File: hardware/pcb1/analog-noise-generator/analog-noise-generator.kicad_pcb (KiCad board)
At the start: 2 copper layers, 12.7 x 55.8 mm, 54 parts, among them J1 USB_C_Receptacle_USB2.0, J2 Conn_01x03, J5 Conn_01x04_Pin, J6 Conn_01x04_Pin, J7 Conn_01x02_Pin, U1 STM32F072CBTx, U2 USBLC6-2SC6, U3 LR8321A-T33, U4 LIS2DH12, U5 LM324

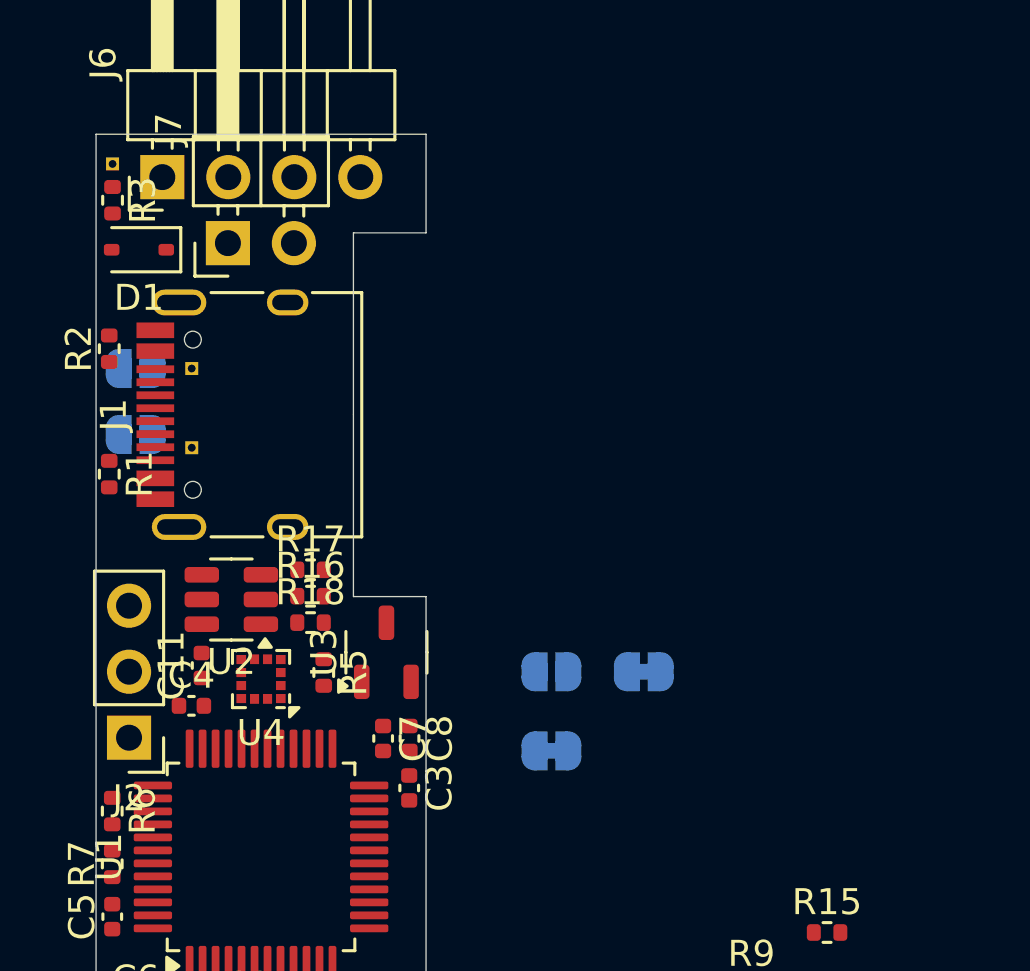
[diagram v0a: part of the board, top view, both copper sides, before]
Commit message: fix some violations
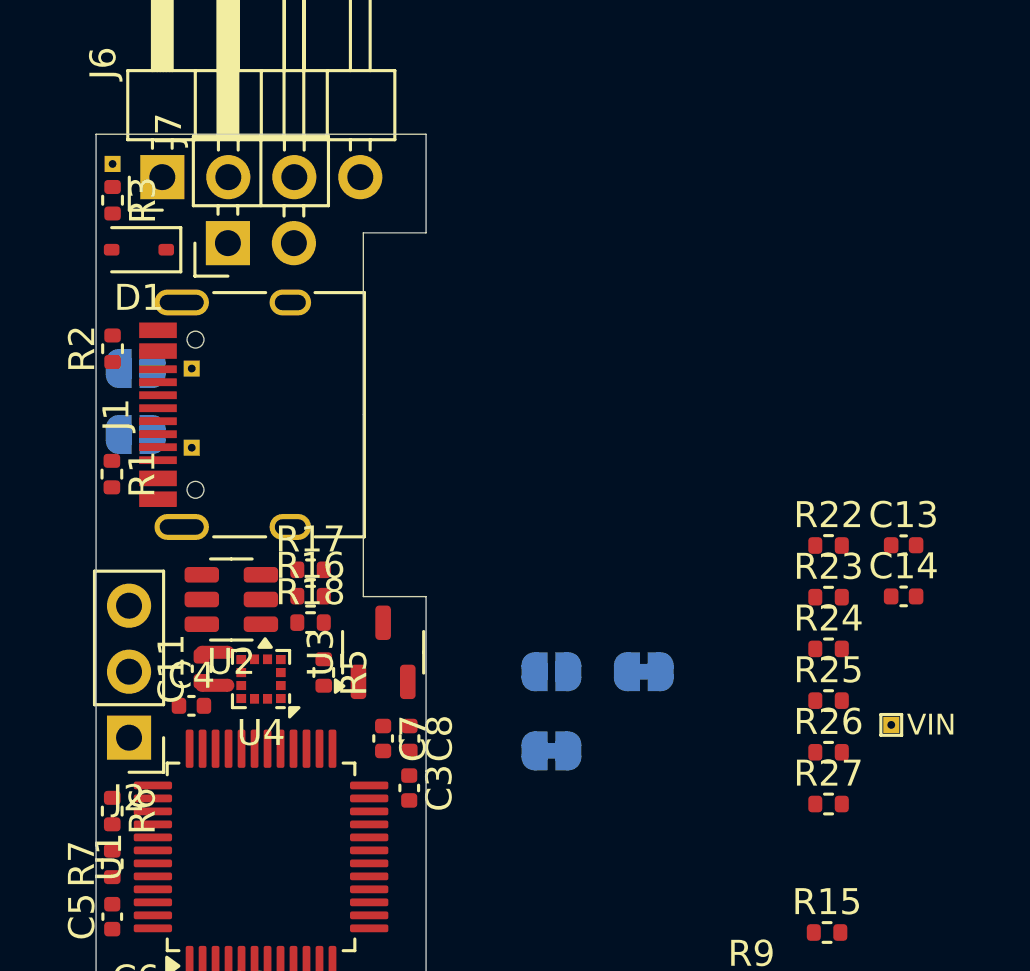
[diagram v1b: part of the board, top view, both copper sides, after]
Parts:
- added C13: 220p, Capacitor_SMD:C_0402_1005Metric, F.Cu at (136.5, 69.5)
- added C14: 220p, Capacitor_SMD:C_0402_1005Metric, F.Cu at (136.5, 71.5)
- added NT1: NetTie_2, NetTie:NetTie-2_SMD_Pad0.5mm, F.Cu at (110.0, 73.7)
- added NT2: NetTie_2, NetTie:NetTie-2_SMD_Pad0.5mm, F.Cu at (110.0, 74.9)
- added R22: 10k, Resistor_SMD:R_0402_1005Metric, F.Cu at (133.6, 69.5)
- added R23: 10k, Resistor_SMD:R_0402_1005Metric, F.Cu at (133.6, 71.5)
- added R24: 10k, Resistor_SMD:R_0402_1005Metric, F.Cu at (133.6, 73.5)
- added R25: 68k, Resistor_SMD:R_0402_1005Metric, F.Cu at (133.6, 75.5)
- added R26: 68k, Resistor_SMD:R_0402_1005Metric, F.Cu at (133.6, 77.5)
- added R27: 10k, Resistor_SMD:R_0402_1005Metric, F.Cu at (133.6, 79.5)
- added TP4: VIN, analog-noise-generator:TestPoint_THTPad_small, F.Cu at (136.0, 76.5)
- moved C11 0.13 mm to (109.5, 74.3)
- moved R2 0.13 mm to (106.0, 62.0)
- moved U3 0.13 mm to (116.5, 73.7)
- moved J1 0.10 mm to (110.3, 64.5)
- moved R1 0.10 mm to (106.0, 66.8)
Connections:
- net Net-(JP4-B) renamed /IMS_SDI
- net Net-(JP6-B) renamed /IMS_SDO
- net Net-(U5C--) renamed /Vmiddle
- R12 pad 1: GND -> +3.3V
- U1 pad 18: unconnected-(U1-PB0-Pad18) -> /IN1L
- U1 pad 19: unconnected-(U1-PB1-Pad19) -> /IN2L
- U1 pad 22: /IMS_INT -> unconnected-(U1-PB11-Pad22)
- U1 pad 30: unconnected-(U1-PA9-Pad30) -> /IMS_INT
- U4 pad 10: +3.3V -> /IMS_3V3
- U4 pad 11: unconnected-(U4-INT2-Pad11) -> /IMS_INT2
- U4 pad 5: GND -> /IMS_GND
- U4 pad 6: GND -> /IMS_GND
- U4 pad 7: GND -> /IMS_GND
- U4 pad 8: GND -> /IMS_GND
- U4 pad 9: +3.3V -> /IMS_3V3
- U5 pad 10: GND -> Net-(U5C-+)
- U5 pad 12: GND -> Net-(U5C-+)
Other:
- outline, holes or cut-outs redrawn

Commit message: continue
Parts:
- removed TP4: VIN, analog-noise-generator:TestPoint_THTPad_small
- moved R27 28.1 mm to (117.0, 56.9)
- moved R26 27.8 mm to (117.3, 55.0), turned to 90 degrees
- moved R25 25.8 mm to (114.8, 57.9), turned to -90 degrees
- moved C13 23.1 mm to (117.5, 82.7), turned to -90 degrees
- moved C14 21.2 mm to (117.5, 80.8), turned to 90 degrees
- moved R24 19.6 mm to (117.5, 84.6), turned to 90 degrees
- moved R16 6.15 mm to (116.5, 77.0), turned to 90 degrees
- moved C7 3.72 mm to (114.2, 74.0)
- moved R5 1.99 mm to (113.7, 72.5), turned to 0 degrees
- moved R18 1.02 mm to (113.7, 71.5)
- moved TP2 0.51 mm to (109.1, 66.3)

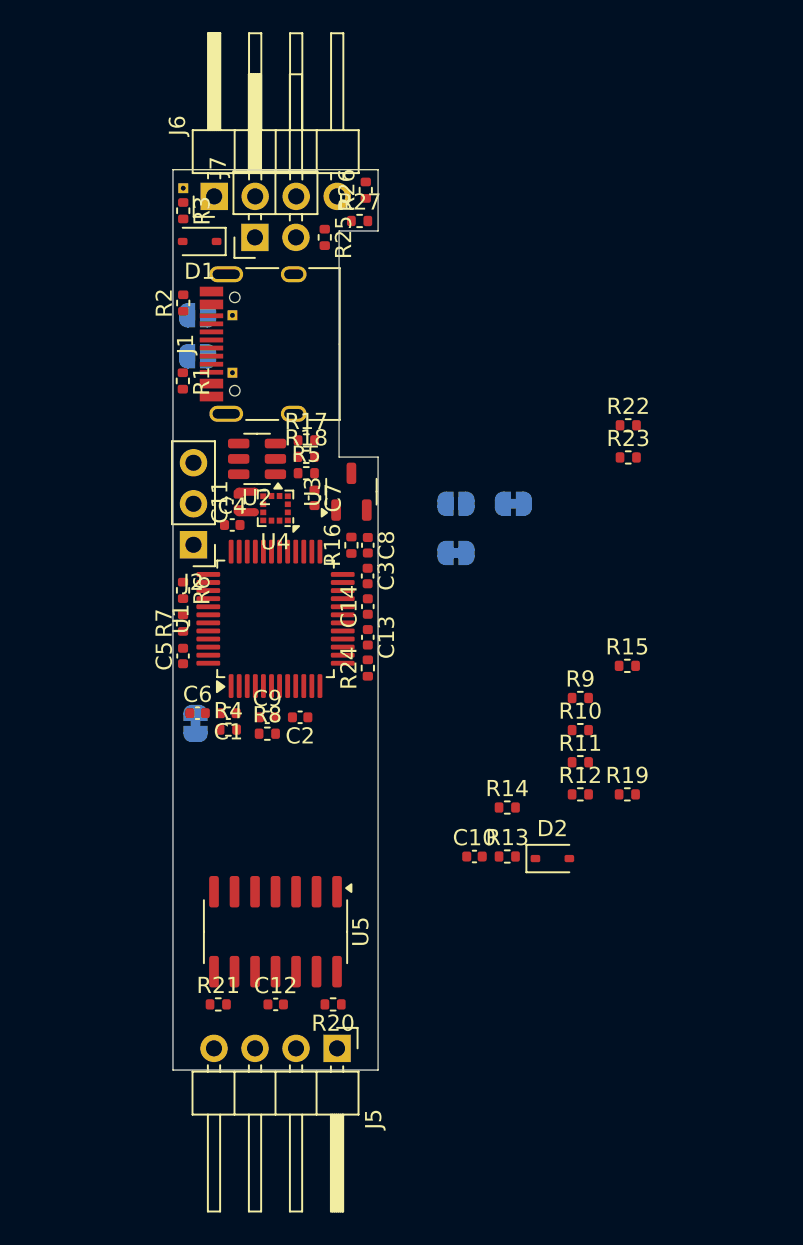
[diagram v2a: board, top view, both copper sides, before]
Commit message: move USB connector to board edge
We had it in the middle to achieve low thickness near the edges
but that's no good if we want it to be usable in any kind of case
(including shrink tube).
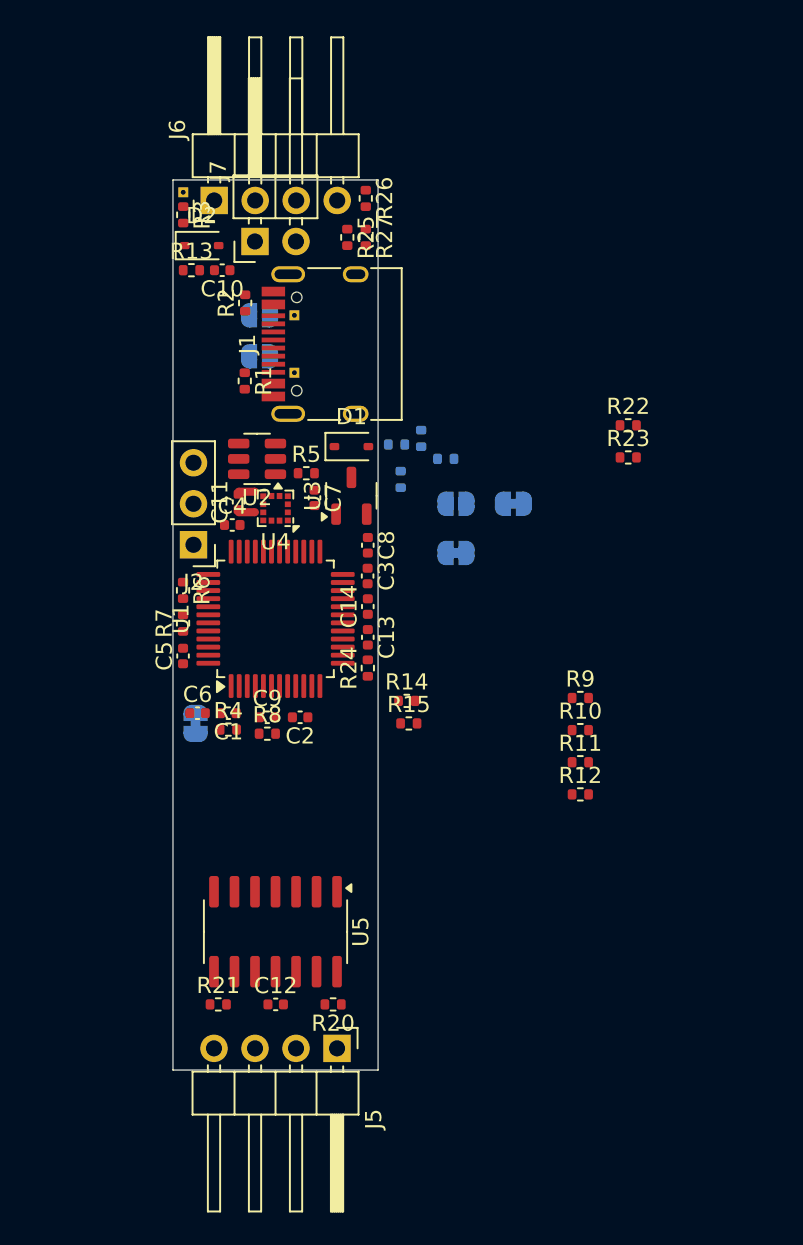
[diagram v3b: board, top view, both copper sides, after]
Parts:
- R16, R17, R18, R19: moved to B.Cu
- moved D2 43.7 mm to (107.2, 58.4)
- moved R13 41.2 mm to (106.6, 59.9)
- moved C10 39.5 mm to (108.5, 59.9), turned to 180 degrees
- moved R19 24.0 mm to (119.5, 72.9), turned to 90 degrees
- moved D1 15.8 mm to (116.5, 70.9), turned to 0 degrees
- moved R15 14.0 mm to (120.0, 88.0)
- moved R14 9.07 mm to (119.9, 86.6)
- moved R17 8.71 mm to (122.3, 71.6), turned to 180 degrees
- moved R16 7.90 mm to (120.8, 70.4)
- moved R18 5.64 mm to (119.3, 70.7), turned to 180 degrees
- moved J1 3.84 mm to (114.2, 64.5)
- moved JP1 3.84 mm to (110.8, 62.7)
- moved JP3 3.84 mm to (110.8, 65.3)
- moved R1 3.84 mm to (109.9, 66.8)
- moved R2 3.84 mm to (109.9, 62.0)
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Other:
- board size 12.7 x 55.8 mm -> 12.7 x 55.1 mm

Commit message: continue
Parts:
- added JP7: SolderJumper_2_Bridged, Jumper:SolderJumper-2_P1.3mm_Bridged_RoundedPad1.0x1.5mm, B.Cu at (102.1, 81.8)
- added R28: 4k7, Resistor_SMD:R_0805_2012Metric_Pad1.20x1.40mm_HandSolder, B.Cu at (98.3, 84.2)
- added R29: 4k7, Resistor_SMD:R_0805_2012Metric_Pad1.20x1.40mm_HandSolder, B.Cu at (98.3, 87.1)
- added TP4: +V, analog-noise-generator:TestPoint_THTPad_small, F.Cu at (126.2, 86.1)
- added TP5: -V, analog-noise-generator:TestPoint_THTPad_small, F.Cu at (126.2, 88.0)
- J2: value Conn_01x03 -> Conn_01x04_Pin; footprint Connector_PinHeader_2.54mm:PinHeader_1x03_P2.54mm_Vertical -> Connector_PinHeader_2.54mm:PinHeader_1x04_P2.54mm_Vertical
- R16, R17, R18, R19: footprint Resistor_SMD:R_0402_1005Metric -> Resistor_SMD:R_0805_2012Metric_Pad1.20x1.40mm_HandSolder
- moved R22 33.3 mm to (120.7, 100.2)
- moved R23 33.3 mm to (120.7, 102.2)
- moved R11 7.06 mm to (123.7, 91.7)
- moved R12 7.06 mm to (123.7, 93.7)
- moved R9 7.06 mm to (123.7, 87.8)
- moved R10 7.06 mm to (123.7, 89.7)
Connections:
- J2 pad 1: GND -> /BOOT0
- J2 pad 2: /SWCLK -> GND
- J2 pad 3: /SWDIO -> /SWCLK
- R6 pad 2: /BOOT0 -> /VUSB_DET
- R7 pad 2: /BOOT0 -> /VUSB_DET
- U1 pad 43: /BOOT0 -> /VUSB_DET

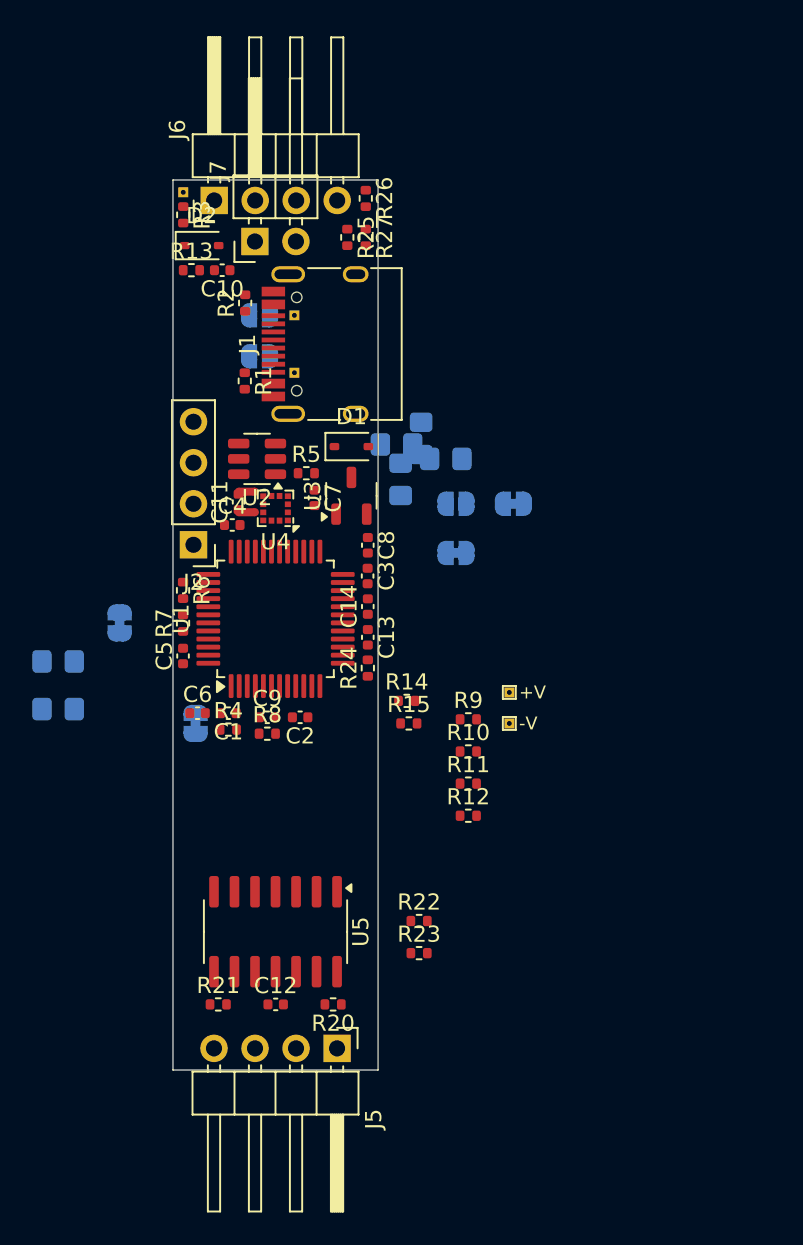
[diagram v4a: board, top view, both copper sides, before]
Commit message: shorten the board a bit
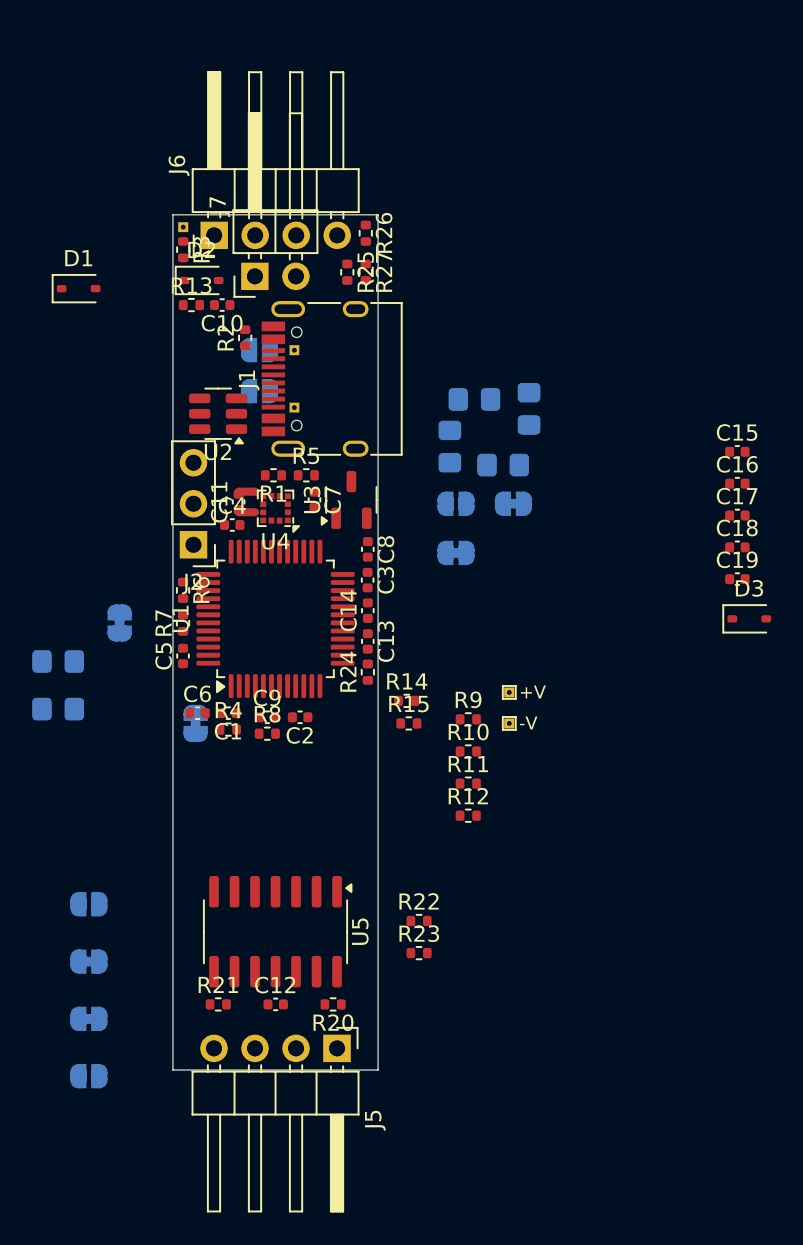
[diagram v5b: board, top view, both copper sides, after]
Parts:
- added C15: 220p, Capacitor_SMD:C_0402_1005Metric, F.Cu at (140.4, 71.2)
- added C16: 100n, 50V, Capacitor_SMD:C_0402_1005Metric, F.Cu at (140.4, 73.2)
- added C17: 100n, 50V, Capacitor_SMD:C_0402_1005Metric, F.Cu at (140.4, 75.1)
- added C18: 220p, Capacitor_SMD:C_0402_1005Metric, F.Cu at (140.4, 77.1)
- added C19: 220p, Capacitor_SMD:C_0402_1005Metric, F.Cu at (140.4, 79.1)
- added D3: ~, Diode_SMD:D_SOD-323, F.Cu at (141.1, 81.5)
- added JP10: SolderJumper_2_Bridged, Jumper:SolderJumper-2_P1.3mm_Bridged_RoundedPad1.0x1.5mm, B.Cu at (100.2, 106.3)
- added JP11: SolderJumper_2_Open, Jumper:SolderJumper-2_P1.3mm_Open_RoundedPad1.0x1.5mm, B.Cu at (100.2, 109.9)
- added JP8: SolderJumper_2_Open, Jumper:SolderJumper-2_P1.3mm_Open_RoundedPad1.0x1.5mm, B.Cu at (100.2, 99.2)
- added JP9: SolderJumper_2_Bridged, Jumper:SolderJumper-2_P1.3mm_Bridged_RoundedPad1.0x1.5mm, B.Cu at (100.2, 102.8)
- C12: value 100n -> 100n, 50V
- J2: value Conn_01x04_Pin -> Conn_01x03_Pin; footprint Connector_PinHeader_2.54mm:PinHeader_1x04_P2.54mm_Vertical -> Connector_PinHeader_2.54mm:PinHeader_1x03_P2.54mm_Vertical
- R14: value 10k -> 68k
- R15: value 5.1k -> 10k
- moved D1 19.5 mm to (99.6, 61.1)
- moved R16 6.93 mm to (127.5, 68.5)
- moved R1 6.11 mm to (111.6, 72.6), turned to 180 degrees
- moved R18 5.58 mm to (124.1, 67.9)
- moved U2 3.69 mm to (108.2, 68.8)
- moved R19 3.66 mm to (122.6, 70.9)
- moved R17 3.58 mm to (125.9, 72.0)
- moved J7 2.16 mm to (110.5, 60.3)
- moved JP1 2.16 mm to (110.8, 64.9)
- moved R2 2.16 mm to (109.9, 64.1)
- moved TP1 2.16 mm to (112.9, 64.9)
- moved TP2 2.16 mm to (112.9, 68.5)
- moved C10 2.16 mm to (108.5, 62.1)
- moved D2 2.16 mm to (107.2, 60.6)
- moved J6 2.16 mm to (108.0, 57.8)
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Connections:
- C10 pad 2: -8V -> -9VA
- C12 pad 1: +3.3V -> Net-(JP8-A)
- C12 pad 2: GND -> Net-(JP10-B)
- D1 pad 1: Net-(D1-K) -> +8V
- D2 pad 2: Net-(D2-A) -> -9VA
- J2 pad 1: /BOOT0 -> GND
- J2 pad 2: GND -> /SWCLK
- J2 pad 3: /SWCLK -> /SWDIO
- J7 pad 1: /VIN -> Net-(J7-Pin_1)
- R11 pad 1: -8V -> -9VA
- R15 pad 1: /VIN_sense -> GND
- R15 pad 2: GND -> /VIN_sense
- R5 pad 1: Net-(D1-K) -> Net-(J7-Pin_1)
- R5 pad 2: +8V -> /VIN
- TP5 pad 1: -8V -> -9VA
- U5 pad 11: GND -> Net-(JP10-B)
- U5 pad 4: +3.3V -> Net-(JP8-A)
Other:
- board size 12.7 x 55.1 mm -> 12.7 x 53 mm

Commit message: continue
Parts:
- removed R13: 100R, Resistor_SMD:R_0402_1005Metric
- added J9: Conn_02x04_Odd_Even, Connector_PinSocket_2.54mm:PinSocket_2x04_P2.54mm_Vertical_SMD, B.Cu at (111.8, 103.0)
- added TP6: TOUCH1, analog-noise-generator:TestPoint_THTPad_small, B.Cu at (106.0, 83.1)
- added TP7: TOUCH2, analog-noise-generator:TestPoint_THTPad_small, B.Cu at (117.5, 82.3)
- R14, R25, R26: footprint Resistor_SMD:R_0402_1005Metric -> Resistor_SMD:R_0603_1608Metric
- moved D3 37.9 mm to (107.2, 64.6), turned to 180 degrees
- moved C16 35.5 mm to (111.8, 94.3)
- moved C17 35.5 mm to (111.8, 96.3)
- moved C19 23.5 mm to (126.8, 98.2)
- moved C15 23.5 mm to (126.8, 90.4)
- moved C18 23.5 mm to (126.8, 96.3)
- moved R5 14.5 mm to (108.0, 59.3), turned to 180 degrees
- moved R24 12.8 mm to (113.7, 72.6), turned to 0 degrees
- moved C13 11.7 mm to (111.8, 72.6), turned to 180 degrees
- moved R26 9.30 mm to (109.6, 62.8), turned to 90 degrees
- moved D1 7.78 mm to (107.2, 62.6), turned to 180 degrees
- moved C10 5.54 mm to (103.3, 64.1)
- moved R1 3.05 mm to (109.0, 71.1)
- moved JP2 2.81 mm to (109.3, 89.3)
- moved R27 2.11 mm to (115.4, 59.3), turned to 0 degrees
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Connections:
- C10 pad 2: -9VA -> -8V
- C19 pad 2: -9VA -> -8V
- D2 pad 2: -9VA -> -8V
- J6 pad 1: /IN1 -> GND
- J6 pad 2: GND -> /VIN'
- J6 pad 3: /IN2 -> GND
- J6 pad 4: GND -> /IN1
- J7 pad 1: Net-(J7-Pin_1) -> /IN2
- JP10 pad 1: -9VA -> -8V
- JP9 pad 2: +9VA -> +8V
- R11 pad 1: -9VA -> -8V
- R5 pad 1: Net-(J7-Pin_1) -> /VIN'
- TP5 pad 1: -9VA -> -8V
- U1 pad 16: unconnected-(U1-PA6-Pad16) -> /TOUCH1
- U1 pad 17: unconnected-(U1-PA7-Pad17) -> /TOUCH2
- U1 pad 2: unconnected-(U1-PC13-Pad2) -> /PUMP_VNEG
- U1 pad 3: unconnected-(U1-PC14-Pad3) -> /EPD_BUSY
- U1 pad 4: unconnected-(U1-PC15-Pad4) -> /EPD_DC
- U1 pad 5: unconnected-(U1-PF0-Pad5) -> /EPD_CS
- U1 pad 6: unconnected-(U1-PF1-Pad6) -> /EPD_RES
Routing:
- net /TOUCH1: track 0.00 -> 40.4 mm, vias 0 -> 1
- net /TOUCH2: track 0.00 -> 38.5 mm
